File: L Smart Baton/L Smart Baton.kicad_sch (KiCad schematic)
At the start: 27 parts, among them J1 USB_C_Receptacle_USB2.0_16P, U1 MDBT50Q-1MV2, U2 LSM6DSOX, U3 BQ24074RGT, U4 TPS63001

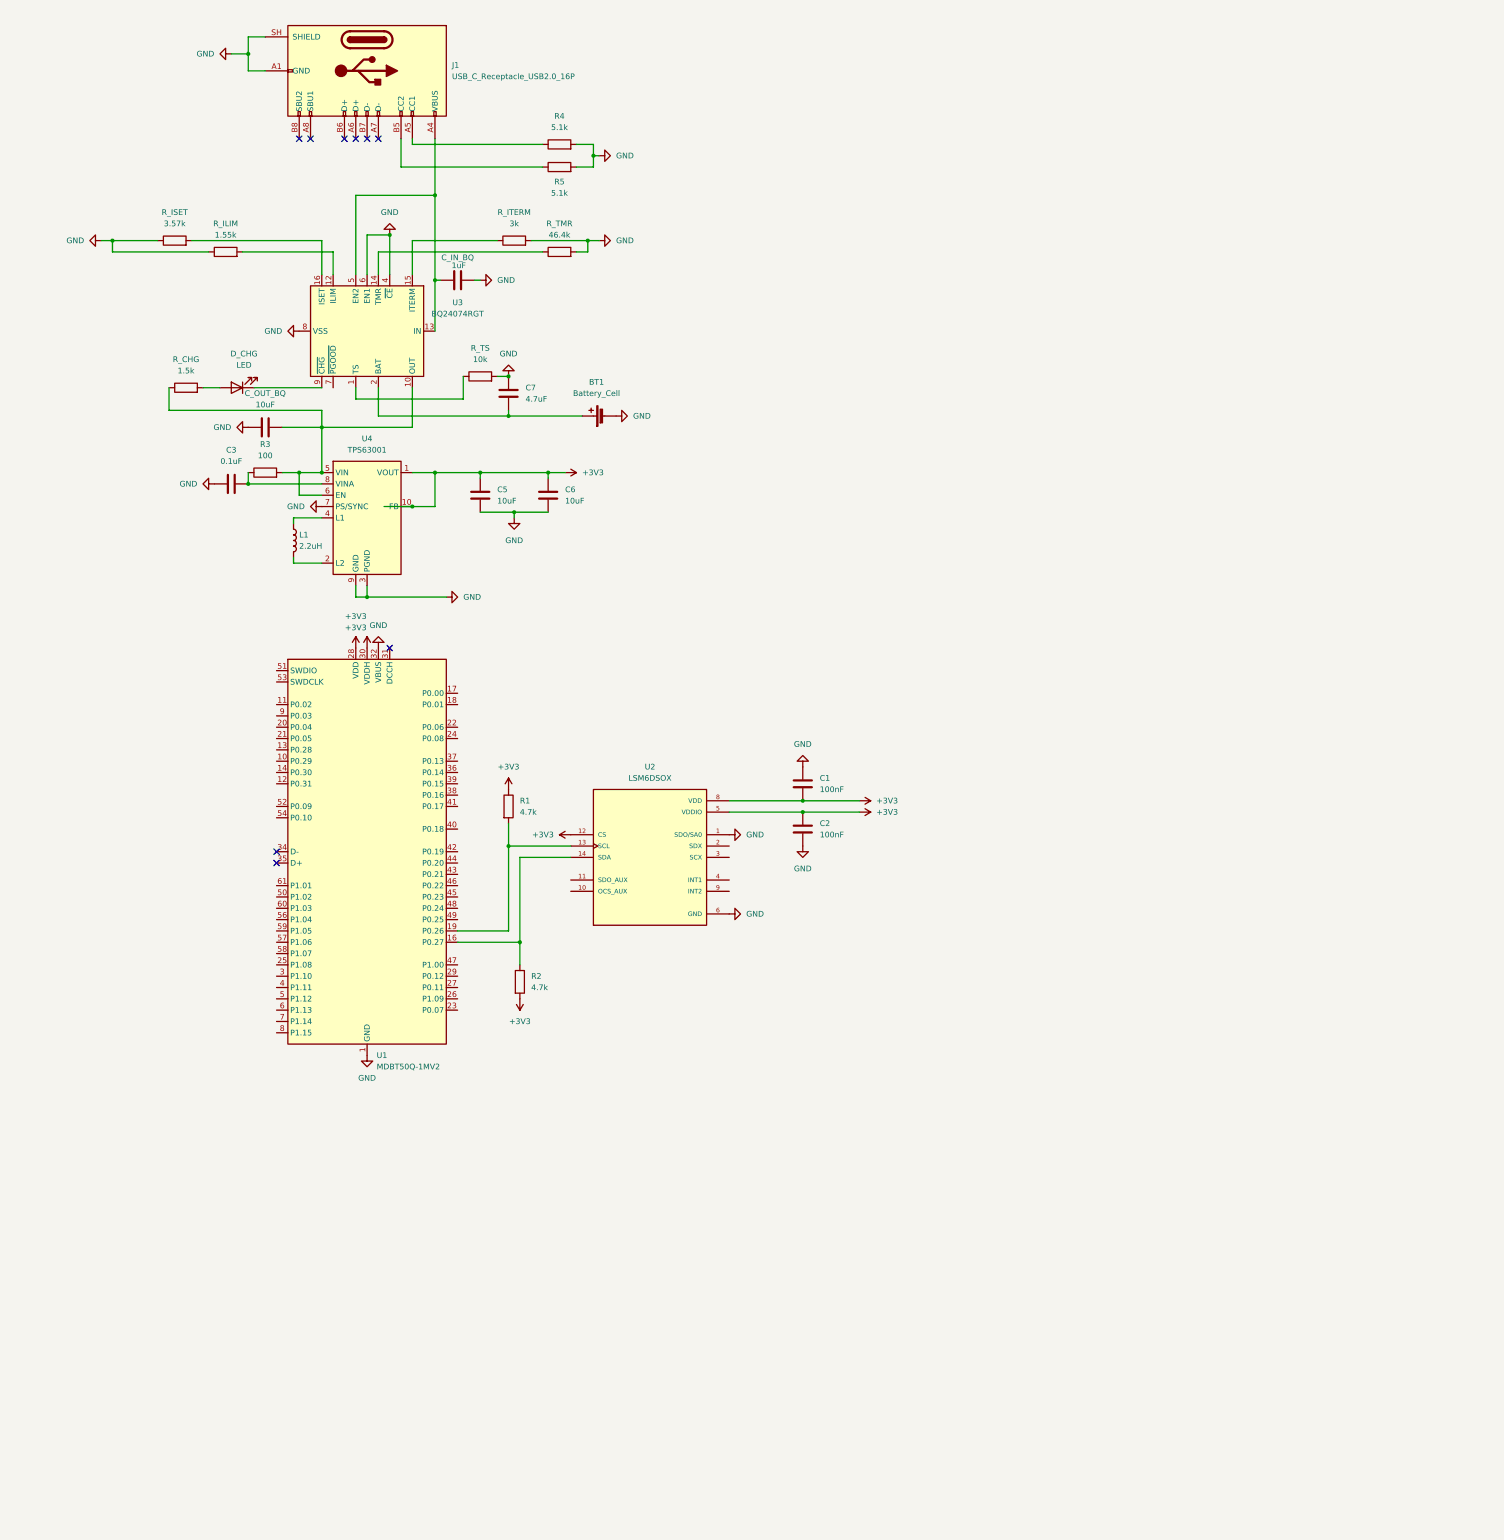
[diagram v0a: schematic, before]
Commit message: LED RGB Switch and voltage sensing added
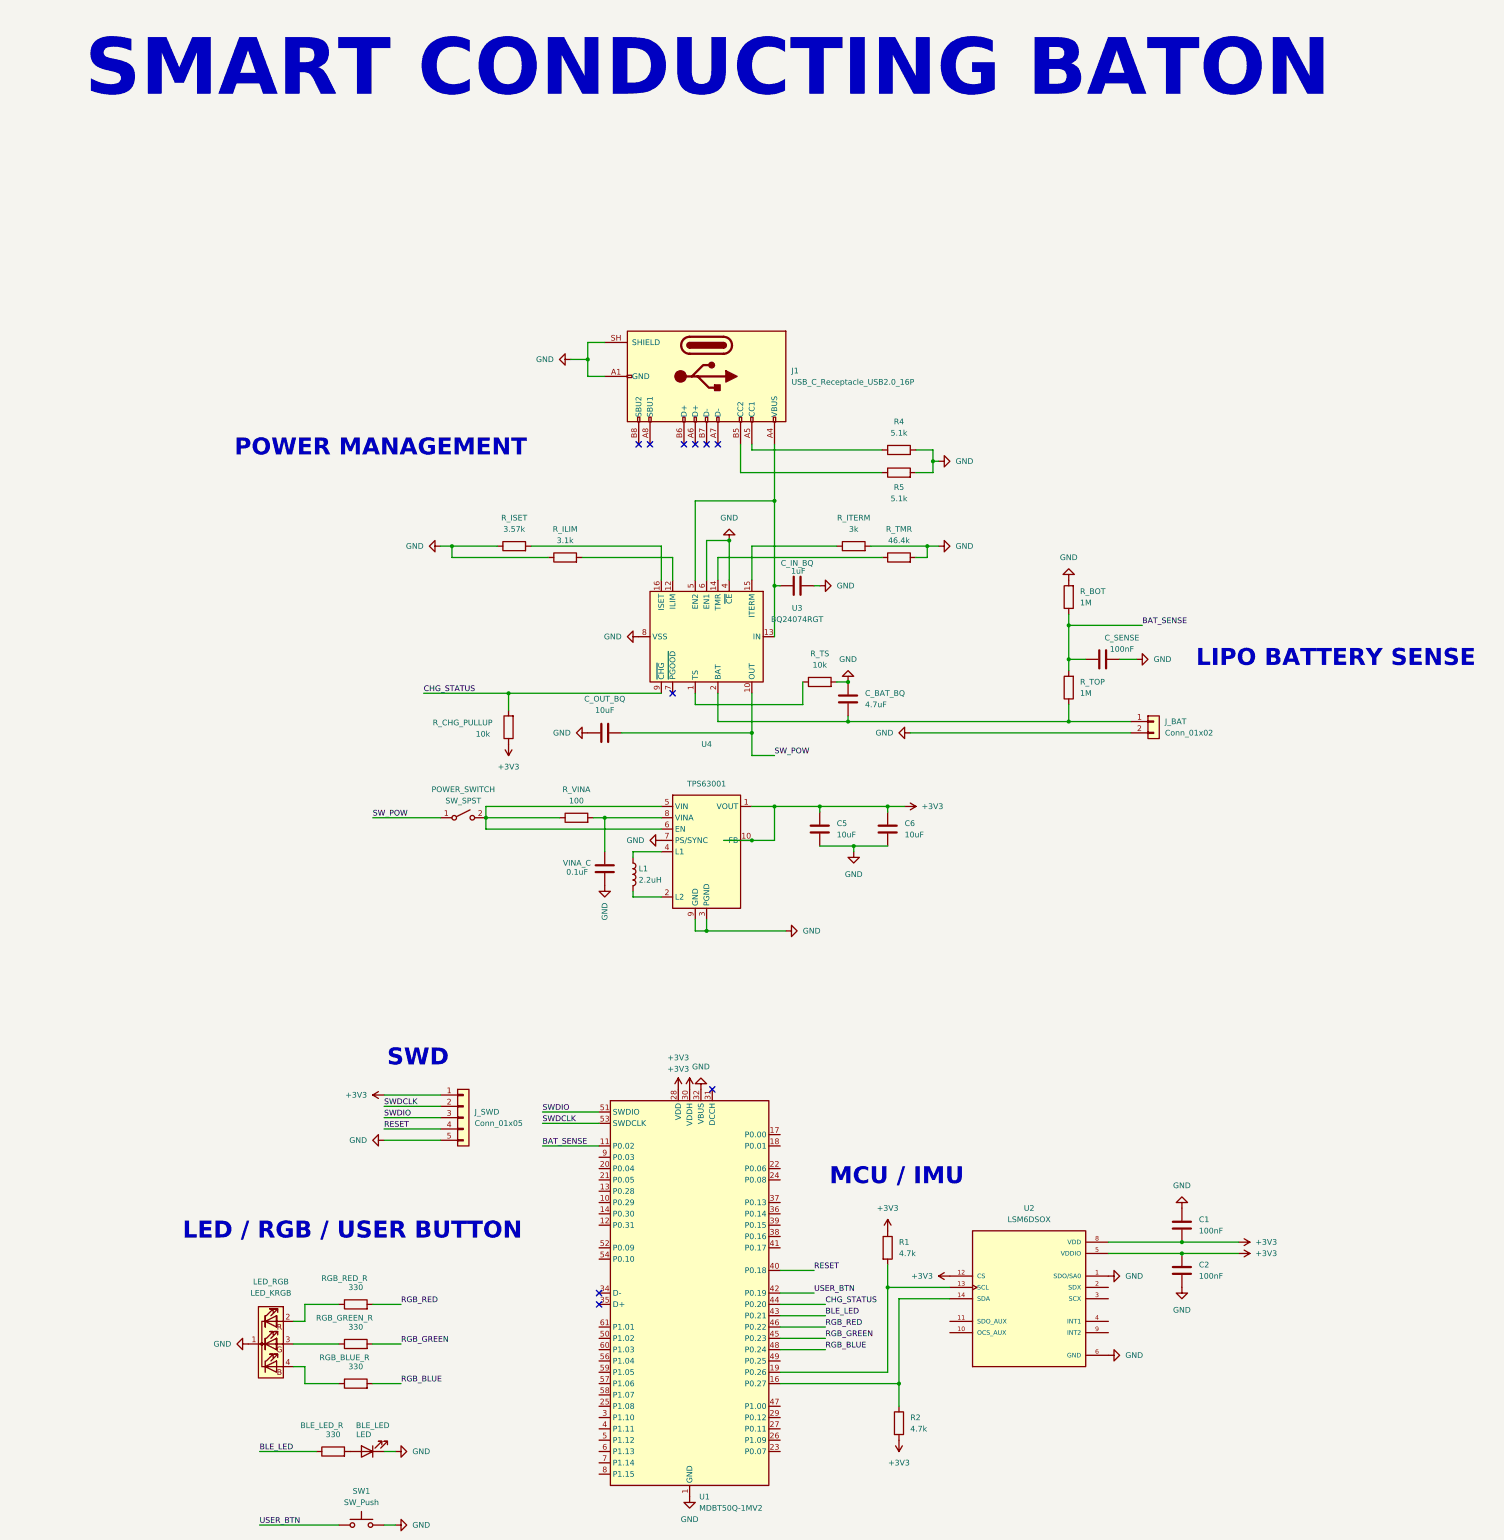
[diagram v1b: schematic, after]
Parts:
- removed BT1: Battery_Cell, symbol Device:Battery_Cell
- removed D_CHG: LED, symbol Device:LED
- removed R3: 100, symbol Device:R
- removed R_CHG: 1.5k, symbol Device:R
- added BLE_LED: LED, symbol Device:LED
- added BLE_LED_R, RGB_BLUE_R, RGB_GREEN_R, RGB_RED_R: 330, symbol Device:R
- added C_SENSE: 100nF, symbol Device:C
- added J_BAT: Conn_01x02, symbol Connector_Generic:Conn_01x02
- added J_SWD: Conn_01x05, symbol Connector_Generic:Conn_01x05
- added LED_RGB: LED_KRGB, symbol Device:LED_KRGB
- added POWER_SWITCH: SW_SPST, symbol Switch:SW_SPST
- added R_BOT, R_TOP: 1M, symbol Device:R
- added R_CHG_PULLUP: 10k, symbol Device:R
- added R_VINA: 100, symbol Device:R
- added SW1: SW_Push, symbol Switch:SW_Push
- R_ILIM: value 1.55k -> 3.1k
- renumbered C7 to C_BAT_BQ, C3 to VINA_C
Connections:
- net +3V3: now also J_SWD.1 (Pin_1), R_CHG_PULLUP.1
- net GND: now also BLE_LED.1 (K), C_SENSE.2, J_BAT.2 (Pin_2), J_SWD.5 (Pin_5), LED_RGB.1 (K), R_BOT.2, SW1.2
- net SW_POW: now reaches C_OUT_BQ.2, U3.10 (OUT), U3.11 (OUT)
- net SW_POW: now also POWER_SWITCH.1 (A); no longer U4.5 (VIN), U4.6 (EN)
- net at U4.8 (VINA), VINA_C.2: now also R_VINA.2
- net at C_BAT_BQ.2, U3.2 (BAT), U3.3 (BAT): now also J_BAT.1 (Pin_1), R_TOP.1
- net CHG_STATUS: now reaches U3.9 (~{CHG})
- net CHG_STATUS: now also U1.44 (P0.20), R_CHG_PULLUP.2
- net BAT_SENSE: now reaches U1.11 (P0.02)
- net BAT_SENSE: now also C_SENSE.1, R_BOT.1, R_TOP.2
- net RESET: now reaches U1.40 (P0.18)
- net RESET: now also J_SWD.4 (Pin_4)
- net USER_BTN: now reaches U1.42 (P0.19)
- net USER_BTN: now also SW1.1
- net BLE_LED: now reaches U1.43 (P0.21)
- net BLE_LED: now also BLE_LED_R.1
- net RGB_GREEN: now reaches U1.45 (P0.23)
- net RGB_GREEN: now also RGB_GREEN_R.2
- net RGB_RED: now reaches U1.46 (P0.22)
- net RGB_RED: now also RGB_RED_R.2
- net RGB_BLUE: now reaches U1.48 (P0.24)
- net RGB_BLUE: now also RGB_BLUE_R.2
- net SWDIO: now reaches U1.51 (SWDIO)
- net SWDIO: now also J_SWD.3 (Pin_3)
- net SWDCLK: now reaches U1.53 (SWDCLK)
- net SWDCLK: now also J_SWD.2 (Pin_2)
- new net: POWER_SWITCH.2 (B), R_VINA.1, U4.5 (VIN), U4.6 (EN)
- new net: LED_RGB.3 (GA), RGB_GREEN_R.1
- new net: LED_RGB.2 (RA), RGB_RED_R.1
- new net: LED_RGB.4 (BA), RGB_BLUE_R.1
- new net: BLE_LED.2 (A), BLE_LED_R.2
- no-connect marks 9 -> 10
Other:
- note added: "LED / RGB / USER BUTTON"
- note added: "LIPO BATTERY SENSE"
- note added: "MCU / IMU"
- note added: "POWER MANAGEMENT"
- note added: "SMART CONDUCTING BATON"
- note added: "SWD"
- moved on the sheet: C1, C2, C5, C6, C_BAT_BQ, C_IN_BQ, C_OUT_BQ, J1, L1, R1, R2, R4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

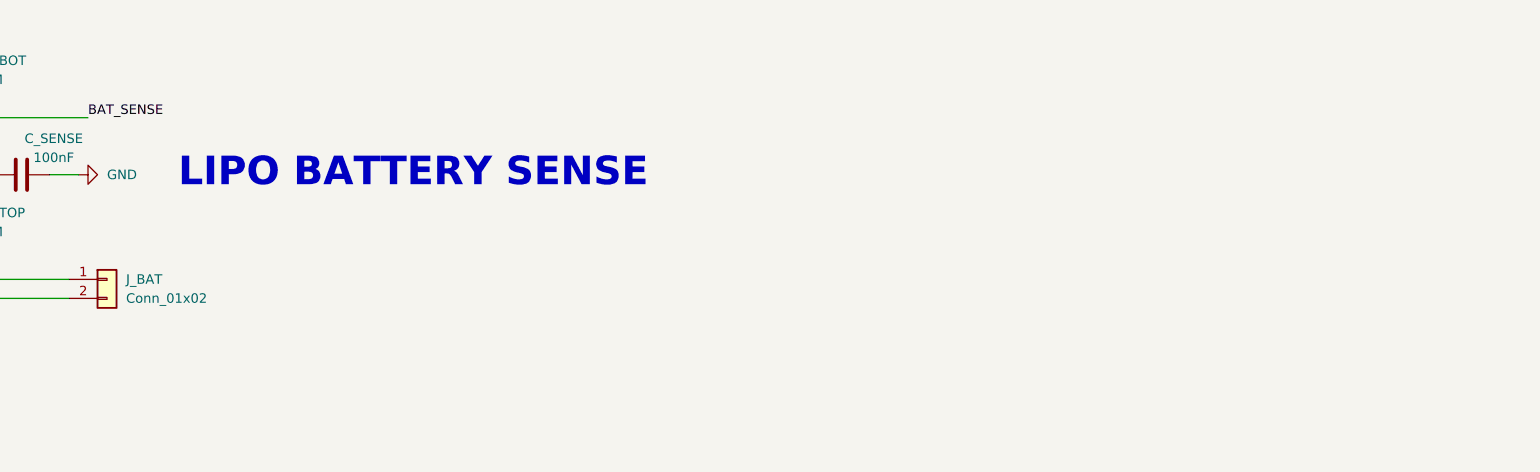
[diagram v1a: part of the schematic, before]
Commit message: comment for lipo battery link
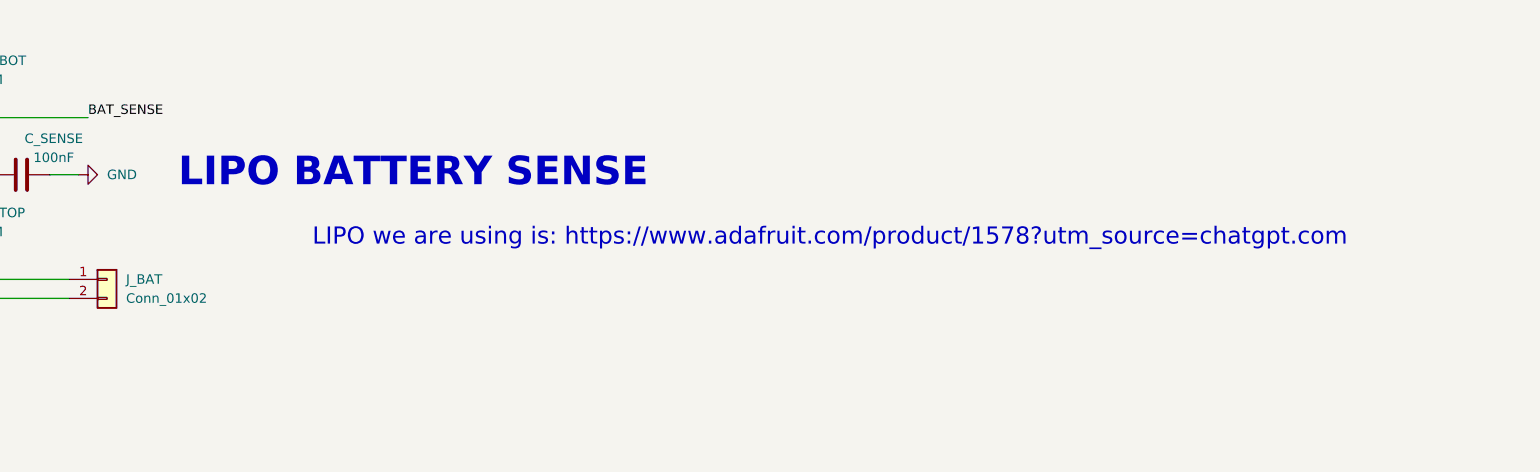
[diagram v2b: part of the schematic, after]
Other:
- note added: "LIPO we are using is: https://www.adafruit.com/product/1578?utm_source=chatgpt.com"
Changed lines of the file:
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@@
+		)
+	)
+	(text "LIPO we are using is: https://www.adafruit.com/product/1578?utm_source=chatgpt.com"
+		(exclude_from_sim no)
+		(at 482.6 176.022 0)
+		(effects
+			(font
+				(size 2.286 2.286)
+			)
 		)
 	)

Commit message: comment fix
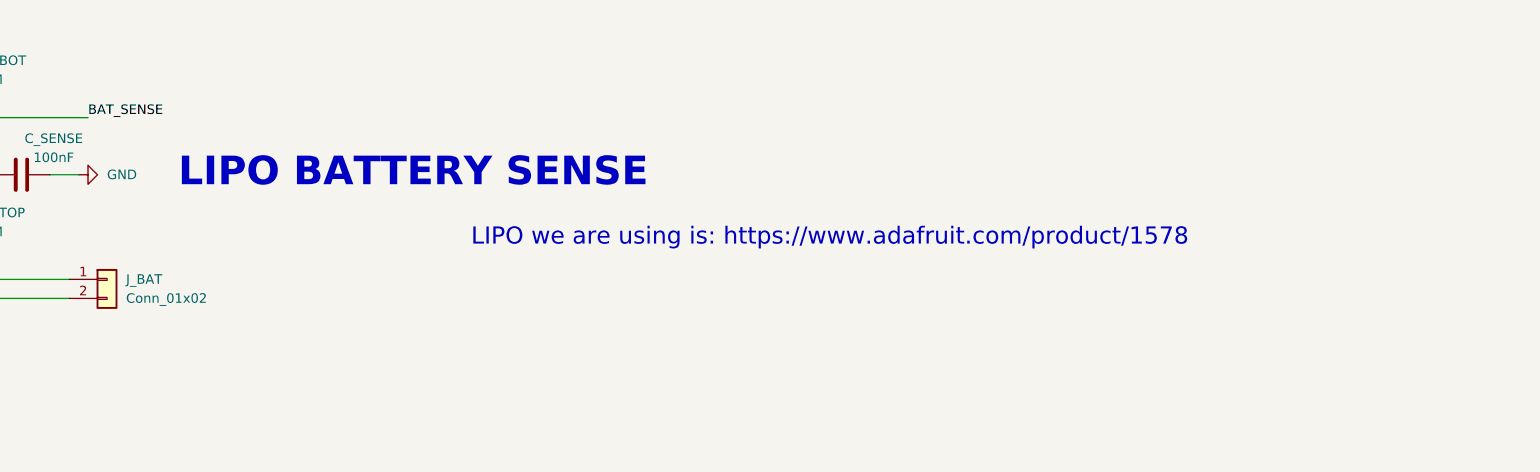
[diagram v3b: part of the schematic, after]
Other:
- note added: "LIPO we are using is: https://www.adafruit.com/product/1578"
- note removed: "LIPO we are using is: https://www.adafruit.com/product/1578?utm_source=chatgpt.com"
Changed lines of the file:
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@@
 		)
 	)
-	(text "LIPO we are using is: https://www.adafruit.com/product/1578?utm_source=chatgpt.com"
+	(text "LIPO we are using is: https://www.adafruit.com/product/1578"
 		(exclude_from_sim no)
 		(at 482.6 176.022 0)

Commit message: finalize smart baton schematic + address fable feedback
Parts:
- removed LED_RGB: LED_KRGB, symbol Device:LED_KRGB
- added +3V3, BAT+1, BQ_OUT1, GND1, VBUS1: TestPoint, TestPoint:TestPoint_Pad_D1.0mm, symbol Connector:TestPoint
- added C_IN_TPS1: 10uF 10V X7R, Capacitor_SMD:C_0805_2012Metric, symbol Device:C
- added C_LFXO1, C_LFXO2: 10pF, Capacitor_SMD:C_0603_1608Metric, symbol Device:C
- added C_MCU_100N1: 100nF, Capacitor_SMD:C_0603_1608Metric, symbol Device:C
- added C_MCU_BULK1: 4.7uF, Capacitor_SMD:C_0805_2012Metric, symbol Device:C
- added LED_RGB1: APFA3010LSEEZGKQBKC, LED_SMD:LED_Kingbright_APFA3010_3x1.5mm_Horizontal, symbol LED:APFA3010
- added R_EN2: 10k, Resistor_SMD:R_0603_1608Metric, symbol Device:R
- added X_LFXO1: FC-135 32.768kHz 7pF, Crystal:Crystal_SMD_3215-2Pin_3.2x1.5mm, symbol Device:Crystal
- C1, C2: footprint (none) -> Capacitor_SMD:C_0603_1608Metric
- C_BAT_BQ1: renamed from C_BAT_BQ; value 4.7uF -> 10uF 10V X7R; footprint (none) -> Capacitor_SMD:C_0805_2012Metric
- C_IN_BQ1: renamed from C_IN_BQ; value 1uF -> 1uF 25V X7R; footprint (none) -> Capacitor_SMD:C_0805_2012Metric
- C_OUT_BQ1: renamed from C_OUT_BQ; value 10uF -> 10uF 10V X7R; footprint (none) -> Capacitor_SMD:C_0805_2012Metric
- C_SENSE1: renamed from C_SENSE; footprint (none) -> Capacitor_SMD:C_0603_1608Metric
- C_TPS_OUT1: renamed from C5; value 10uF -> 22uF 10V X7R; footprint (none) -> Capacitor_SMD:C_0805_2012Metric
- C_TPS_OUT2: renamed from C6; value 10uF -> 22uF 10V X7R; footprint (none) -> Capacitor_SMD:C_0805_2012Metric
- D1: renamed from BLE_LED; value LED -> APT1608QBC/D; footprint (none) -> LED_SMD:LED_0603_1608Metric
- J1: value USB_C_Receptacle_USB2.0_16P -> USB4105-GF-A; footprint (none) -> Connector_USB:USB_C_Receptacle_GCT_USB4105-xx-A_16P_TopMnt_Horizontal
- J_BAT1: renamed from J_BAT; footprint (none) -> Connector_JST:JST_PH_B2B-PH-K_1x02_P2.00mm_Vertical
- J_SWD1: renamed from J_SWD; value Conn_01x05 -> 22052051; footprint (none) -> Connector_PinHeader_2.54mm:PinHeader_1x05_P2.54mm_Horizontal
- L1: value 2.2uH -> 74438335022; footprint (none) -> Inductor_SMD:L_Wuerth_MAPI-3015
- POWER_SWITCH1: renamed from POWER_SWITCH; value SW_SPST -> JS102011SAQN; footprint (none) -> Button_Switch_SMD:SW_SPDT_CK_JS102011SAQN; symbol Switch:SW_SPST -> Switch:SW_SPDT
- R1, R2, R4, R5: footprint (none) -> Resistor_SMD:R_0603_1608Metric
- R3: renamed from BLE_LED_R; footprint (none) -> Resistor_SMD:R_0603_1608Metric
- RGB_BLUE_R1: renamed from RGB_RED_R; footprint (none) -> Resistor_SMD:R_0603_1608Metric
- RGB_GREEN_R1: renamed from RGB_GREEN_R; footprint (none) -> Resistor_SMD:R_0603_1608Metric
- RGB_RED_R1: renamed from RGB_BLUE_R; value 330 -> 750; footprint (none) -> Resistor_SMD:R_0603_1608Metric
- R_BOT1: renamed from R_TOP; footprint (none) -> Resistor_SMD:R_0603_1608Metric
- R_CHG_PULLUP1: renamed from R_CHG_PULLUP; footprint (none) -> Resistor_SMD:R_0603_1608Metric
- R_ILIM1: renamed from R_ILIM; value 3.1k -> 3.09k; footprint (none) -> Resistor_SMD:R_0603_1608Metric
- R_ISET1: renamed from R_ISET; footprint (none) -> Resistor_SMD:R_0603_1608Metric
- R_ITERM1: renamed from R_ITERM; footprint (none) -> Resistor_SMD:R_0603_1608Metric
- R_TMR1: renamed from R_TMR; footprint (none) -> Resistor_SMD:R_0603_1608Metric
- R_TOP1: renamed from R_BOT; footprint (none) -> Resistor_SMD:R_0603_1608Metric
- R_TS1: renamed from R_TS; footprint (none) -> Resistor_SMD:R_0603_1608Metric
- R_VINA1: renamed from R_VINA; footprint (none) -> Resistor_SMD:R_0603_1608Metric
- SW1: value SW_Push -> B3U-1000P; footprint (none) -> Button_Switch_SMD:SW_SPST_B3U-1000P
- VINA_C1: renamed from VINA_C; footprint (none) -> Capacitor_SMD:C_0603_1608Metric
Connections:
- net +3V3: now also +3V3.1, C_MCU_100N1.2, C_MCU_BULK1.2, LED_RGB1.2 (A)
- net GND: now also U2.2 (SDX), U2.3 (SCX), C_IN_TPS1.1, C_LFXO1.2, C_LFXO2.1, C_MCU_100N1.1, C_MCU_BULK1.1, GND1.1
- net RGB_BLUE: now also RGB_BLUE_R1.2; no longer RGB_RED_R1.2
- net RGB_RED: now also RGB_RED_R1.2; no longer RGB_BLUE_R1.2
- net SW_POW: now also POWER_SWITCH1.2 (B), BQ_OUT1.1; no longer POWER_SWITCH1.1 (A)
- net at R_VINA1.1, U4.5 (VIN), U4.6 (EN): now also POWER_SWITCH1.1 (A), C_IN_TPS1.2; no longer POWER_SWITCH1.2 (B)
- net at RGB_GREEN_R1.1: now also LED_RGB1.3 (G)
- net at RGB_BLUE_R1.1: now also LED_RGB1.4 (B)
- net at RGB_RED_R1.1: now also LED_RGB1.1 (R)
- net at C_BAT_BQ1.2, J_BAT1.1 (Pin_1), R_BOT1.1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: now also BAT+1.1
- net IMU_INT1: now reaches U2.4 (INT1)
- net IMU_INT1: now also U1.37 (P0.13)
- net IMU_INT2: now reaches U2.9 (INT2)
- net IMU_INT2: now also U1.36 (P0.14)
- net at C_IN_BQ1.1, J1.A4 (VBUS), J1.A9 (VBUS)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: now also R_EN2.1, VBUS1.1; no longer U3.5 (EN2)
- net at U1.17 (P0.00): now also C_LFXO1.1, X_LFXO1.1
- net at U1.18 (P0.01): now also C_LFXO2.2, X_LFXO1.2
- new net: R_EN2.2, U3.5 (EN2)
- no-connect marks 10 -> 47
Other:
- note added: "Crystal"
- moved on the sheet: C_TPS_OUT1, C_TPS_OUT2, L1, R_VINA1, U4, VINA_C1
